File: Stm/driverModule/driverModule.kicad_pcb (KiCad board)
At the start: 2 copper layers, 40 parts, among them J101 Conn_02x13_Odd_Even, J102 AXK520147YG, J103 Conn_02x08_Odd_Even, J104 AXK520147YG, J201 Conn_02x05_Row_Letter_First, J202 Conn_01x04_Pin, Q1 BSS138, Q2 BSS138, Q201 AO3400A, U1 TLE94103EP, U102 ADM7171ACPZ-3.0-R7, U103 TJA1051T-3, U104 TPS5410DR, U105 SN74LV165APWR, U106 SN74LV165APWR, U201 DRV8838, U204 VNH5019A-E

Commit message: Symbols
Changed some symbols
Components placements
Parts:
- removed J201: Conn_02x05_Row_Letter_First, Connector_PinHeader_2.54mm:PinHeader_2x07_P2.54mm_Vertical
- removed Q201: AO3400A, Package_TO_SOT_SMD:SOT-23
- removed U105, U106: SN74LV165APWR, Package_SO:TSSOP-16_4.4x5mm_P0.65mm
- added C202: 47uF, Capacitor_SMD:CP_Elec_6.3x5.4_Nichicon, F.Cu at (129.7, 101.8)
- added J1: Conn_02x05_Odd_Even, Connector_PinHeader_2.54mm:PinHeader_2x05_P2.54mm_Vertical, F.Cu at (150.6, 85.1)
- added Q3: AON7410, Local_Footprints:DFN_3X3_EP, F.Cu at (142.9, 111.0)
- added U101: 74HC165, Package_SO:TSSOP-16_4.4x5mm_P0.65mm, F.Cu at (192.4, 79.4)
- added U107: 74HC165, Package_SO:TSSOP-16_4.4x5mm_P0.65mm, F.Cu at (202.6, 79.4)
- moved J104 115.5 mm to (196.2, 109.9), turned to 90 degrees
- moved J102 86.8 mm to (166.2, 109.9), turned to 90 degrees
- moved C101 84.1 mm to (122.1, 82.4)
- moved C102 84.1 mm to (122.7, 89.3)
- moved C103 84.1 mm to (125.9, 86.7)
- moved C104 84.1 mm to (121.6, 71.7)
- moved C105 84.1 mm to (112.5, 85.9)
- moved C106 84.1 mm to (133.5, 76.3)
- moved D101 84.1 mm to (130.1, 67.9)
- moved L101 84.1 mm to (112.5, 71.3)
- moved R101 84.1 mm to (122.1, 80.6)
- moved R102 84.1 mm to (125.3, 80.6)
- moved U102 84.1 mm to (122.4, 85.9)
- moved U104 84.1 mm to (127.3, 76.0)
- moved J202 65.2 mm to (110.7, 124.2), turned to 90 degrees
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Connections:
- net Net-(U204-CS) renamed /Motors/CS
- net Net-(U204-EN/DIAGA) renamed /Motors/EN/DIAGA
- net Net-(U204-EN/DIAGB) renamed /Motors/EN/DIAGB
- net Net-(U204-INA) renamed /Motors/INA
- net Net-(U204-INB) renamed /Motors/INB
- U1 pad 6: /Motors/MirrorMotroXYB -> /Motors/MirrorMotorXYB
- U204 pad 11: Net-(Q201-G) -> /Motors/G
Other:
- copper layers 2 -> 4

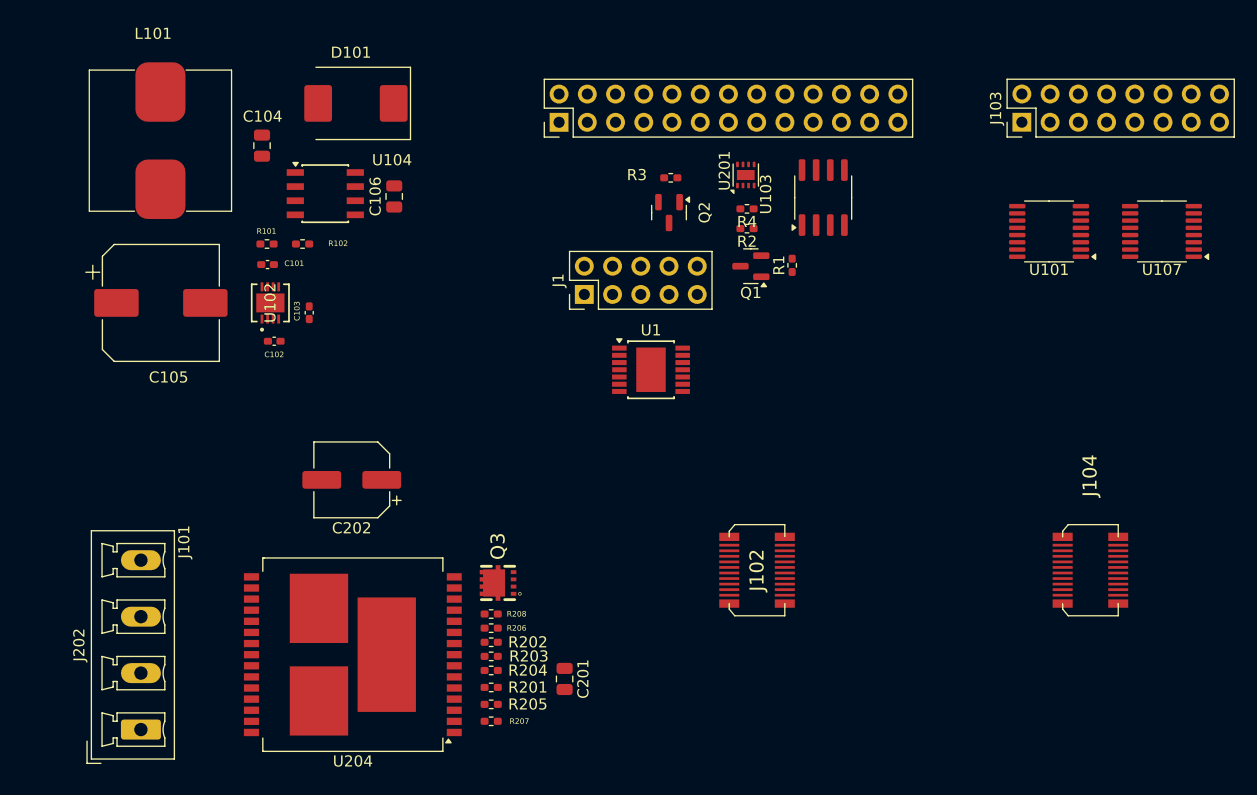
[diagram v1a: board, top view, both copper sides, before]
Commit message: 3d Models
Added Some 3d Models
And remove some components from schematic
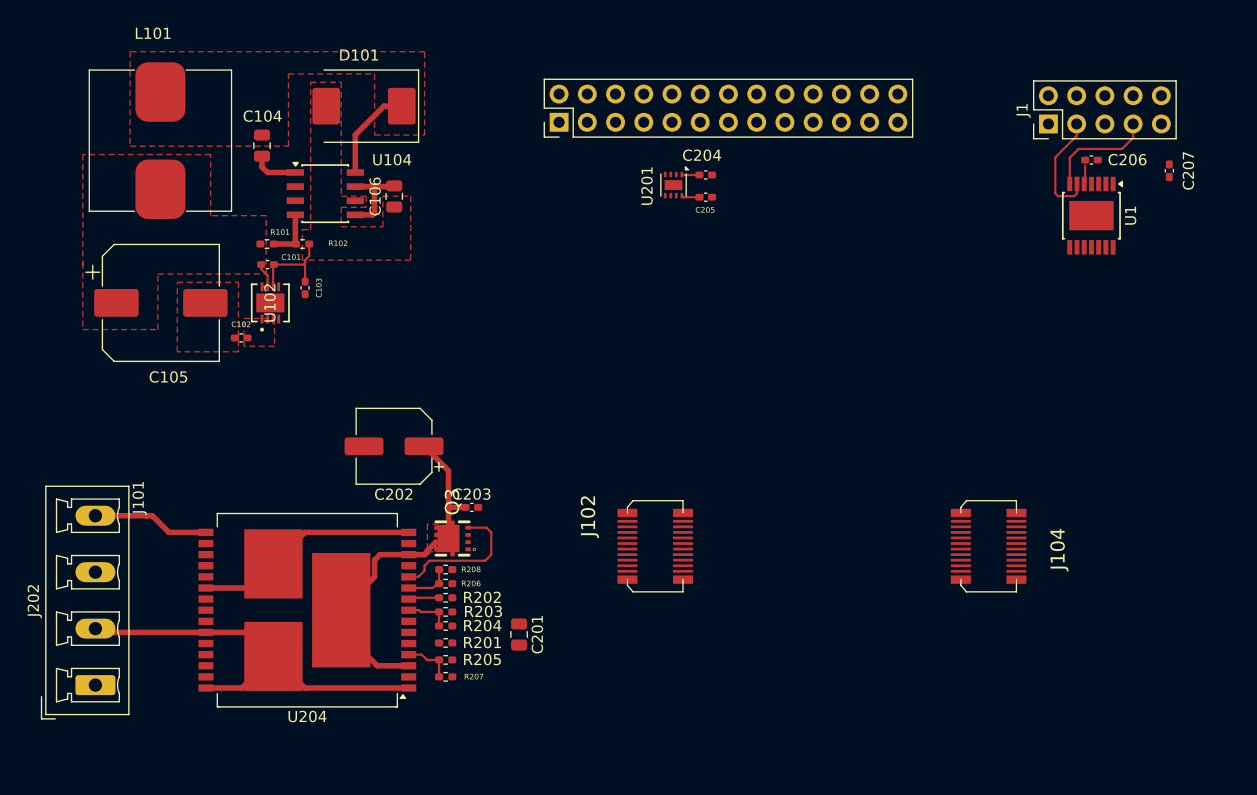
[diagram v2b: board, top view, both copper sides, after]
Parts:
- removed J103: Conn_02x08_Odd_Even, Connector_PinHeader_2.54mm:PinHeader_2x08_P2.54mm_Vertical
- removed Q1, Q2: BSS138, Package_TO_SOT_SMD:SOT-23
- removed R1, R2: 10K, Resistor_SMD:R_0402_1005Metric_Pad0.72x0.64mm_HandSolder
- removed R3, R4: R_US, Resistor_SMD:R_0402_1005Metric_Pad0.72x0.64mm_HandSolder
- removed U101, U107: 74HC165, Package_SO:TSSOP-16_4.4x5mm_P0.65mm
- removed U103: TJA1051T-3, Package_SO:SOIC-8_3.9x4.9mm_P1.27mm
- added C203: 0.1uF, Capacitor_SMD:C_0402_1005Metric_Pad0.74x0.62mm_HandSolder, F.Cu at (140.5, 104.2)
- added C204: 0u1F, Capacitor_SMD:C_0402_1005Metric_Pad0.74x0.62mm_HandSolder, F.Cu at (161.6, 74.3)
- added C205: 0u1F, Capacitor_SMD:C_0402_1005Metric_Pad0.74x0.62mm_HandSolder, F.Cu at (161.6, 76.3)
- added C206: 0u1F, Capacitor_SMD:C_0402_1005Metric_Pad0.74x0.62mm_HandSolder, F.Cu at (196.2, 73.0)
- added C207: 0u1F, Capacitor_SMD:C_0402_1005Metric_Pad0.74x0.62mm_HandSolder, F.Cu at (203.3, 74.0)
- moved J1 44.5 mm to (192.4, 69.8)
- moved U1 42.0 mm to (196.2, 78.0), turned to -90 degrees
- moved J102 9.41 mm to (157.0, 107.8)
- moved J104 9.41 mm to (187.0, 107.8)
- moved U201 6.56 mm to (158.7, 75.2), turned to -90 degrees
- moved C201 5.73 mm to (144.8, 115.7)
- moved R202 5.73 mm to (138.1, 112.4)
- moved R204 5.73 mm to (138.1, 114.9)
- moved R206 5.73 mm to (138.1, 111.1)
- moved J202 5.73 mm to (106.6, 120.2)
- moved Q3 5.73 mm to (138.8, 107.0)
- moved R201 5.73 mm to (138.1, 116.4)
- moved R203 5.73 mm to (138.1, 113.7)
- moved R205 5.73 mm to (138.1, 118.0)
- moved R207 5.73 mm to (138.1, 119.5)
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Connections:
- J102 pad 16: /Inhibit -> GND
- U1 pad 15: (no net) -> unconnected-(U1-EDP-Pad15)
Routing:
- net /Motors/WindwoMotorA: track 0.00 -> 37.7 mm
- net /Motors/Vout: track 0.00 -> 32.6 mm
- net /Motors/WindowMotorB: track 0.00 -> 30.9 mm
- net /Motors/G: track 0.00 -> 12.8 mm
- net +12V: track 0.00 -> 11.0 mm
- net /Motors/MirrorMotorXYB: track 0.00 -> 10.1 mm
- net /Motors/MirrorMotorYA: track 0.00 -> 10.0 mm
- net /PH: track 0.00 -> 8.64 mm
- net GND: track 0.00 -> 8.44 mm
- net /VSENSE: track 0.00 -> 4.65 mm
- net /Motors/INA: track 0.00 -> 4.47 mm
- net /BOOT: track 0.00 -> 4.17 mm
- net /Motors/INB: track 0.00 -> 4.16 mm
- net /Motors/CS: track 0.00 -> 4.06 mm
- net /Motors/EN/DIAGB: track 0.00 -> 2.77 mm
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- added copper zone on F.Cu, net +3V3
- added copper zone on F.Cu, net +5V
- added copper zone on F.Cu, net /Motors/Vout
- added copper zone on F.Cu, net /PH
- added copper zone on F.Cu, net GND

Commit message: Routing
Finish some routing
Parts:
- added C1: 0u1F, Capacitor_SMD:C_0402_1005Metric_Pad0.74x0.62mm_HandSolder, F.Cu at (188.5, 98.0)
- added C2: 0u1F, Capacitor_SMD:C_0402_1005Metric_Pad0.74x0.62mm_HandSolder, F.Cu at (188.5, 99.6)
- added C3: 0u1F, Capacitor_SMD:C_0402_1005Metric_Pad0.74x0.62mm_HandSolder, F.Cu at (188.5, 112.6)
- added C4: 0u1F, Capacitor_SMD:C_0402_1005Metric_Pad0.74x0.62mm_HandSolder, F.Cu at (188.5, 111.1)
- added J103: Conn_02x08_Odd_Even, Connector_PinHeader_2.54mm:PinHeader_2x08_P2.54mm_Vertical, F.Cu at (199.4, 101.1)
- added U101: 74HC165, Package_SO:TSSOP-16_4.4x5mm_P0.65mm, F.Cu at (191.5, 104.6)
- added U107: 74HC165, Package_SO:TSSOP-16_4.4x5mm_P0.65mm, F.Cu at (191.5, 117.6)
- moved J102 18.6 mm to (150.3, 90.4)
- moved J104 18.6 mm to (180.3, 90.4)
- moved C207 9.80 mm to (194.6, 78.5)
- moved C204 5.77 mm to (156.1, 72.4)
- moved C205 5.77 mm to (156.1, 74.4)
- moved C206 5.77 mm to (190.8, 71.1)
- moved J1 5.77 mm to (186.9, 67.8)
- moved J101 5.77 mm to (142.9, 67.7)
- moved U1 5.77 mm to (190.8, 76.1)
- moved U201 5.77 mm to (153.2, 73.3)
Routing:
- net SpiClock: track 0.00 -> 82.6 mm, vias 0 -> 4
- net MirrorSpiChipSelect: track 0.00 -> 63.3 mm, vias 0 -> 2
- net /ParallelLoad: track 0.00 -> 58.8 mm, vias 0 -> 2
- net WindowMotorDirA: track 0.00 -> 38.9 mm
- net WindowMotorPWM: track 0.00 -> 38.6 mm
- net SpiMasterInput: track 0.00 -> 34.0 mm, vias 0 -> 2
- net WindowMotorCurrentSense: track 0.00 -> 34.0 mm
- net WindowMotorDirB: track 0.00 -> 29.1 mm
- net SpiMasterOutput: track 0.00 -> 27.4 mm, vias 0 -> 1
- net /LatchSensorGreenConnector: track 0.00 -> 25.2 mm, vias 0 -> 1
- net /SerialOut: track 0.00 -> 19.7 mm, vias 0 -> 2
- net /Motors/MirrorMotorXA: track 0.00 -> 19.6 mm, vias 0 -> 1
- net nSleep: track 0.00 -> 15.9 mm
- net LatchMotorB: track 0.00 -> 15.8 mm, vias 0 -> 1
- net LatchMotorDirection: track 0.00 -> 15.3 mm
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
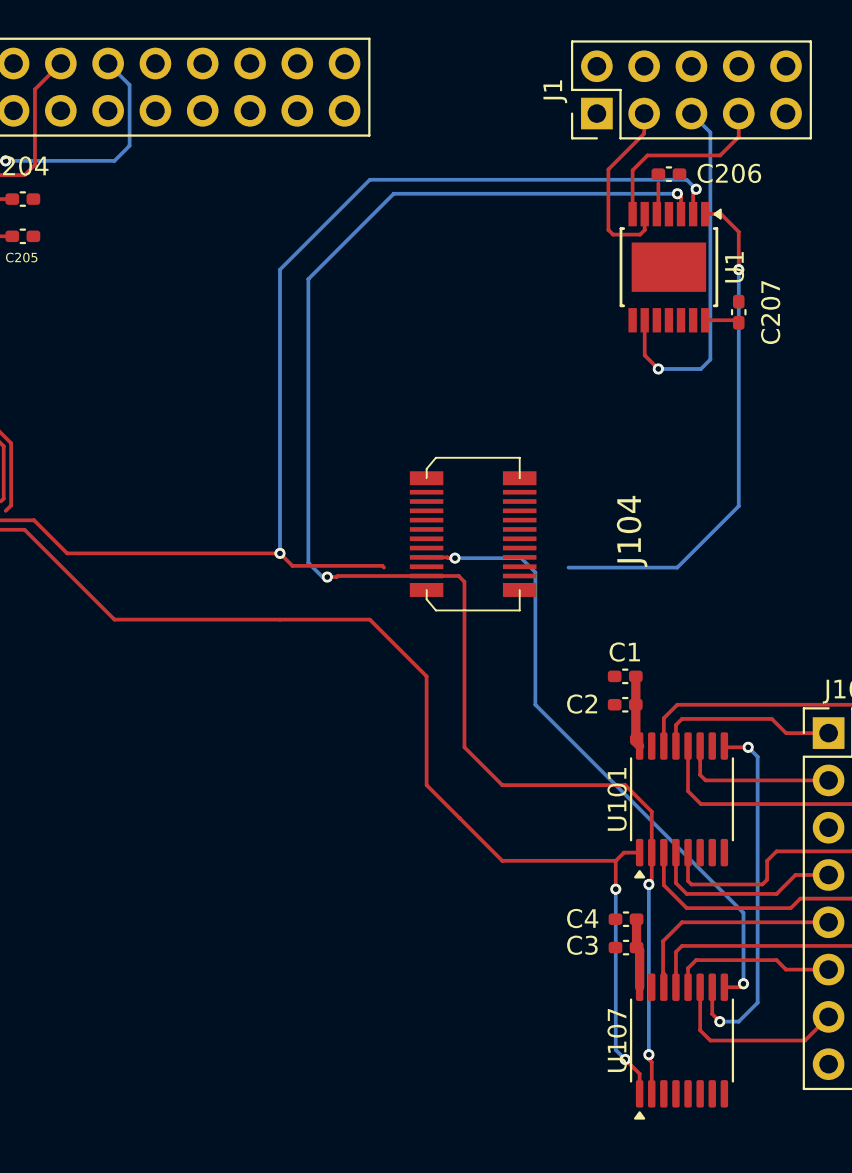
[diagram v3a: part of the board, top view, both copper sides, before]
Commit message: Changed Connector
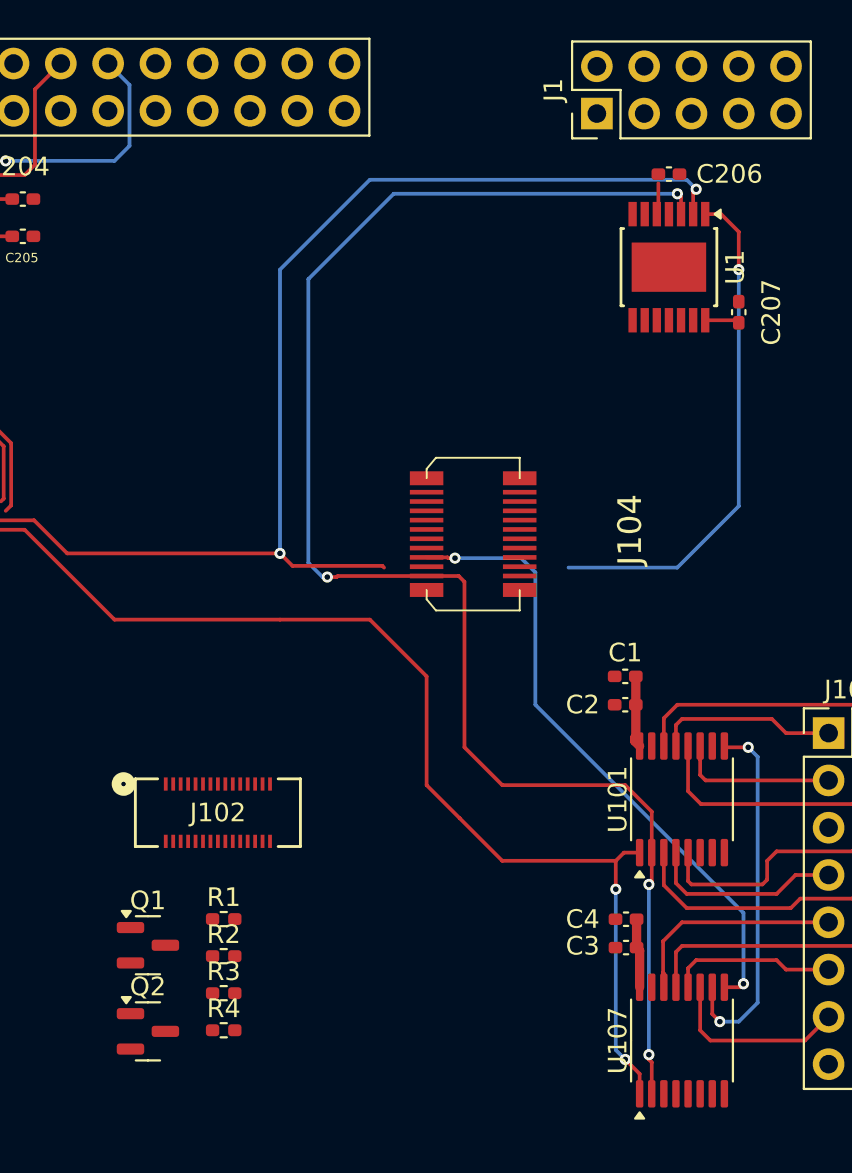
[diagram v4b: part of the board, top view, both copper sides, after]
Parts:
- added J102: DF40HC3.5-30DS-0.4V51, con-hirose-df40:CONN_DF40HC3.5-30DS-0.4V51_HIR, F.Cu at (166.6, 105.4)
- added Q1: BSS138, Package_TO_SOT_SMD:SOT-23, F.Cu at (162.8, 112.5)
- added Q2: BSS138, Package_TO_SOT_SMD:SOT-23, F.Cu at (162.8, 117.1)
- added R1: 10K, Resistor_SMD:R_0402_1005Metric_Pad0.72x0.64mm_HandSolder, F.Cu at (166.9, 111.1)
- added R2: 10K, Resistor_SMD:R_0402_1005Metric_Pad0.72x0.64mm_HandSolder, F.Cu at (166.9, 113.1)
- added R3: R_US, Resistor_SMD:R_0402_1005Metric_Pad0.72x0.64mm_HandSolder, F.Cu at (166.9, 115.1)
- added R4: R_US, Resistor_SMD:R_0402_1005Metric_Pad0.72x0.64mm_HandSolder, F.Cu at (166.9, 117.0)
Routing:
- net /Motors/MirrorMotorXA: track 19.6 -> 0.00 mm, vias 1 -> 0
- net /Motors/MirrorMotorXYB: track 10.1 -> 0.00 mm
- net /Motors/MirrorMotorYA: track 10.0 -> 0.00 mm

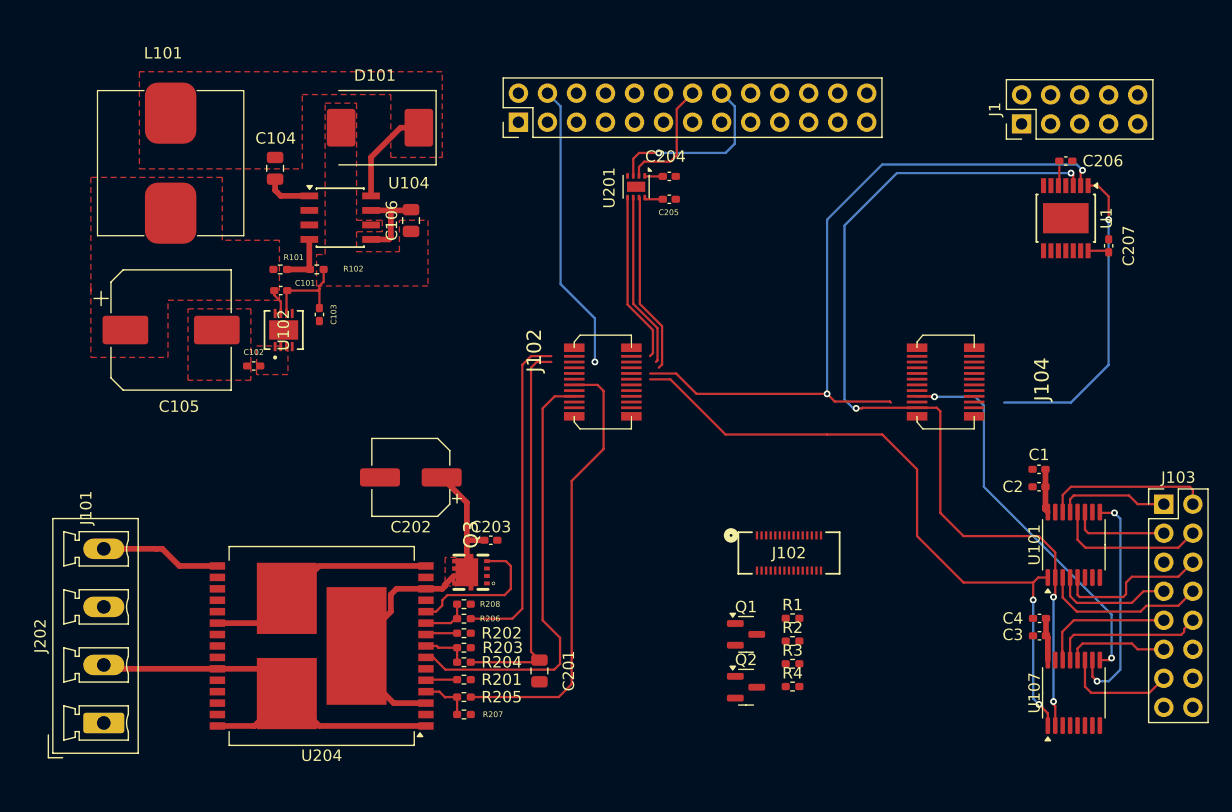
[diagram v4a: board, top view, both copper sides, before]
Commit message: PCB Board
PCB board created, need to verify connectors polarity
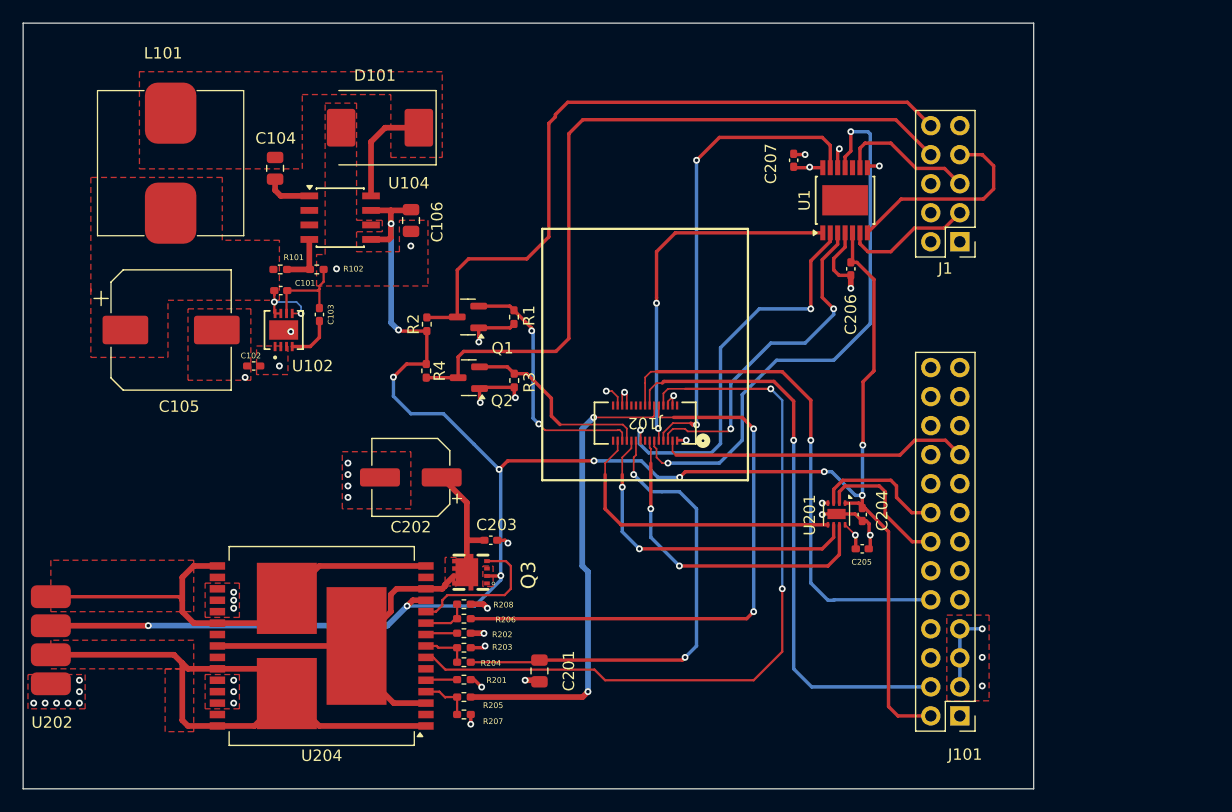
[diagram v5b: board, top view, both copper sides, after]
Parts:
- removed C1, C2, C3, C4: 0u1F, Capacitor_SMD:C_0402_1005Metric_Pad0.74x0.62mm_HandSolder
- removed the J102 at (150.3, 90.4)
- removed J103: Conn_02x08_Odd_Even, Connector_PinHeader_2.54mm:PinHeader_2x08_P2.54mm_Vertical
- removed J104: AXK520147YG, Local_Footprints:AXK520147YG
- removed J202: Conn_01x04_Pin, Connector_Phoenix_MC_HighVoltage:PhoenixContact_MCV_1,5_4-G-5.08_1x04_P5.08mm_Vertical
- removed U101, U107: 74HC165, Package_SO:TSSOP-16_4.4x5mm_P0.65mm
- added U202: ~, Local_Footprints:HeaderMotorCustomeSMD, F.Cu at (102.0, 113.0)
- moved J101 64.7 mm to (181.5, 119.6), turned to 180 degrees
- moved R2 42.3 mm to (134.9, 85.3), turned to 90 degrees
- moved R4 42.3 mm to (134.8, 89.4), turned to -90 degrees
- moved Q1 36.9 mm to (138.5, 84.7), turned to 180 degrees
- moved Q2 36.4 mm to (138.6, 90.0), turned to 180 degrees
- moved R1 35.9 mm to (142.5, 84.7), turned to 90 degrees
- moved C205 34.9 mm to (173.0, 105.0)
- moved R3 34.7 mm to (142.6, 90.3), turned to 90 degrees
- moved C204 34.1 mm to (173.0, 102.0), turned to -90 degrees
- moved U201 33.6 mm to (170.8, 102.0)
- moved C207 28.6 mm to (167.0, 71.0)
- moved C206 21.0 mm to (172.0, 80.5), turned to -90 degrees
- moved U1 19.4 mm to (171.5, 74.5), turned to 90 degrees
- moved J102 17.0 mm to (154.0, 94.0), turned to 180 degrees
- moved J1 11.6 mm to (181.5, 78.1), turned to 180 degrees
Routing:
- net +12V: track 11.0 -> 177.2 mm, vias 0 -> 12
- net /Motors/KeyFobClose12V: track 0.00 -> 66.4 mm
- net /Motors/keyFobOpen12V: track 0.00 -> 61.1 mm
- net /ParallelLoad: track 58.8 -> 0.00 mm, vias 2 -> 0
- net SpiClock: track 82.6 -> 30.1 mm, vias 4 -> 2
- net MirrorMotorsEnable: track 0.00 -> 49.6 mm, vias 0 -> 2
- net /LatchSensorPurpleConnector: track 0.00 -> 45.3 mm, vias 0 -> 1
- net GND: track 8.44 -> 41.6 mm, vias 0 -> 37
- net WindowMotorPWM: track 38.6 -> 67.1 mm, vias 0 -> 2
- net MirrorSpiChipSelect: track 63.3 -> 35.1 mm
- net /LatchPositionThroughSignal: track 0.00 -> 27.3 mm
- net /LatchSensorGreenConnector: track 25.2 -> 51.1 mm
- net KeyfobOpen3v3: track 0.00 -> 22.4 mm, vias 0 -> 2
- net WindowMotorDirB: track 29.1 -> 50.7 mm, vias 0 -> 2
- net /SerialOut: track 19.7 -> 0.00 mm, vias 2 -> 0
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- added copper zone on F.Cu, net +12V
- added copper zone on In2.Cu, net +3V3
- added copper zone on F.Cu, net /Motors/WindowMotorB
- added copper zone on F.Cu, net /Motors/WindwoMotorA
- added copper zone on In1.Cu, net GND
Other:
- board outline added: 88.4 x 67 mm

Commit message: 3d Symbols
Update 3d symbols
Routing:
- net GND: track 41.6 -> 47.1 mm, vias 37 -> 42
- net /Motors/WindowMotorB: track 41.9 -> 42.8 mm
- net +12V: track 177.2 -> 177.8 mm
